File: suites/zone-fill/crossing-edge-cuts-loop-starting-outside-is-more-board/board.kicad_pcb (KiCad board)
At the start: 2 copper layers, 16 x 18 mm, 3 parts

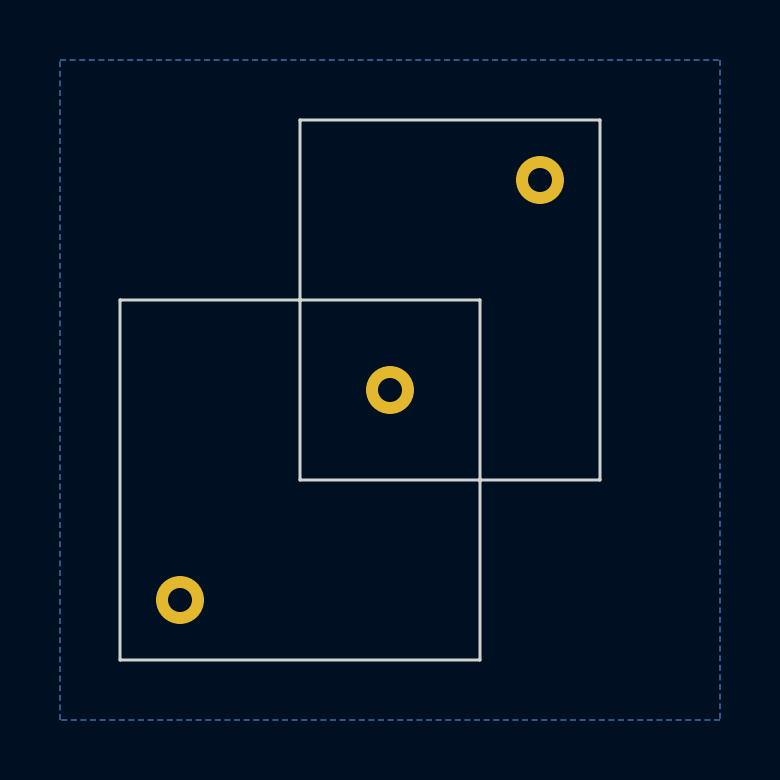
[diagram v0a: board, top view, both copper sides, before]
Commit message: zone-fill: the two crossing-loop cases at a hairline min_thickness, so the outline rule is compared alone
At 0.25 mm both boards carried the fill opening's own nanometre residue at
the notch's re-entrant corner beside the outline behaviour they exist to pin;
at 0.001 mm the opening is a no-op. The union case also drops its pads: with
none, island removal keeps every area, and a pad's relief cut no longer splits
a run of the far boundary.
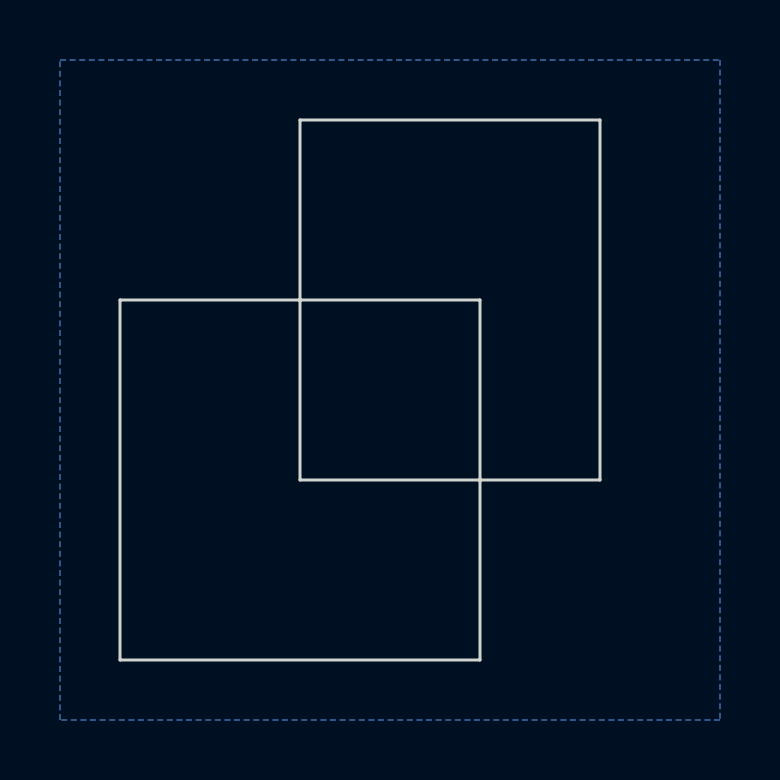
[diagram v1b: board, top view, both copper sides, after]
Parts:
- removed ? (x3): , anchor:pad
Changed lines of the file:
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@@
 	(gr_rect (start 4 10) (end 16 22) (stroke (width 0.1) (type default)) (layer "Edge.Cuts") (fill no))
 	(gr_rect (start 10 4) (end 20 16) (stroke (width 0.1) (type default)) (layer "Edge.Cuts") (fill no))
-	(footprint "anchor:pad"
-		(layer "B.Cu")
-		(at 6 20)
-		(pad "1" thru_hole circle (at 0 0) (size 1.6 1.6) (drill 0.8) (layers "*.Cu" "*.Mask") (net 1 "GND"))
-	)
-	(footprint "anchor:pad"
-		(layer "B.Cu")
-		(at 18 6)
-		(pad "1" thru_hole circle (at 0 0) (size 1.6 1.6) (drill 0.8) (layers "*.Cu" "*.Mask") (net 1 "GND"))
-	)
-	(footprint "anchor:pad"
-		(layer "B.Cu")
-		(at 13 13)
-		(pad "1" thru_hole circle (at 0 0) (size 1.6 1.6) (drill 0.8) (layers "*.Cu" "*.Mask") (net 1 "GND"))
-	)
 	(zone
 		(net 1)
@@
 		(hatch edge 0.5)
 		(connect_pads (clearance 0.2))
-		(min_thickness 0.25)
+		(min_thickness 0.001)
 		(fill yes (thermal_gap 0.5) (thermal_bridge_width 0.5))
 		(polygon (pts (xy 2 2) (xy 24 2) (xy 24 24) (xy 2 24)))
